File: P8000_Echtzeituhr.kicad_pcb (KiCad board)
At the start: 2 copper layers, 106.7 x 40.6 mm, 36 parts, among them X1 Socket-DIN41612-96Pin-3row

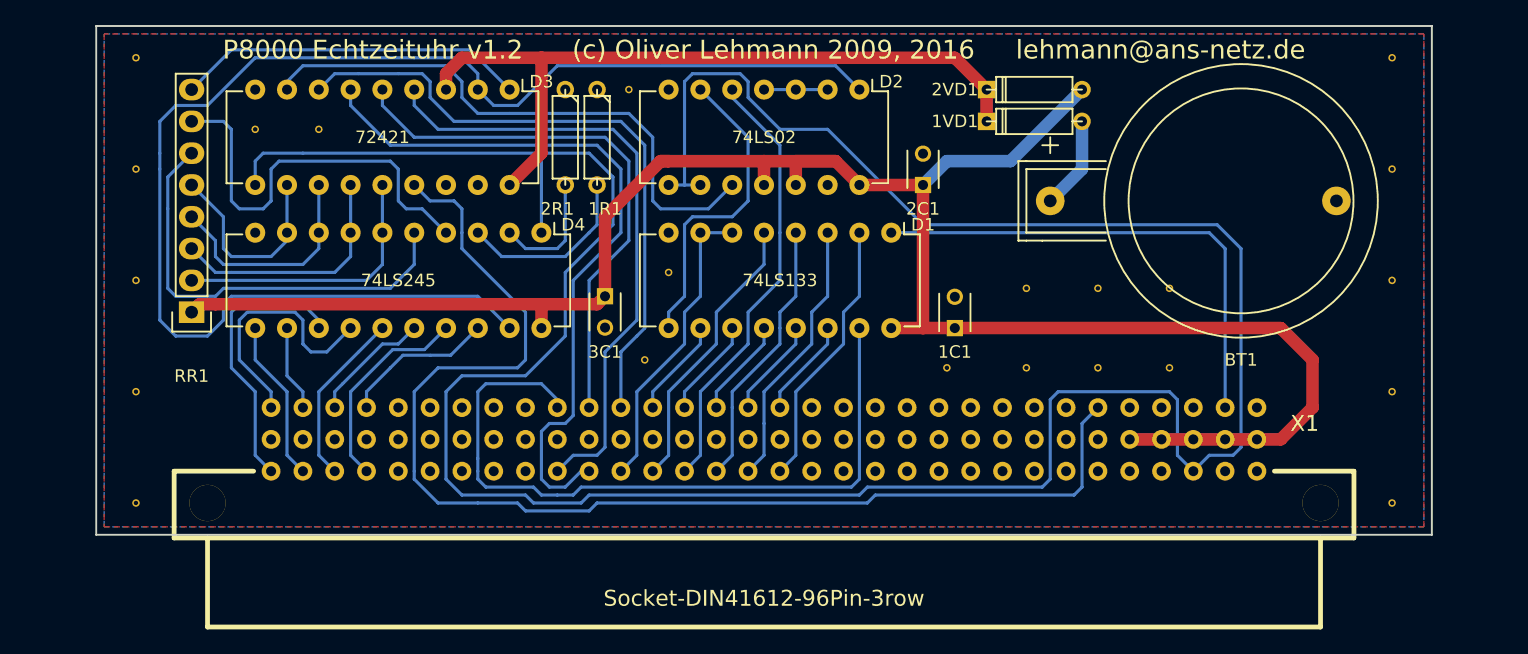
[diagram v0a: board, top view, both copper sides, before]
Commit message: fix errors from version 1.1
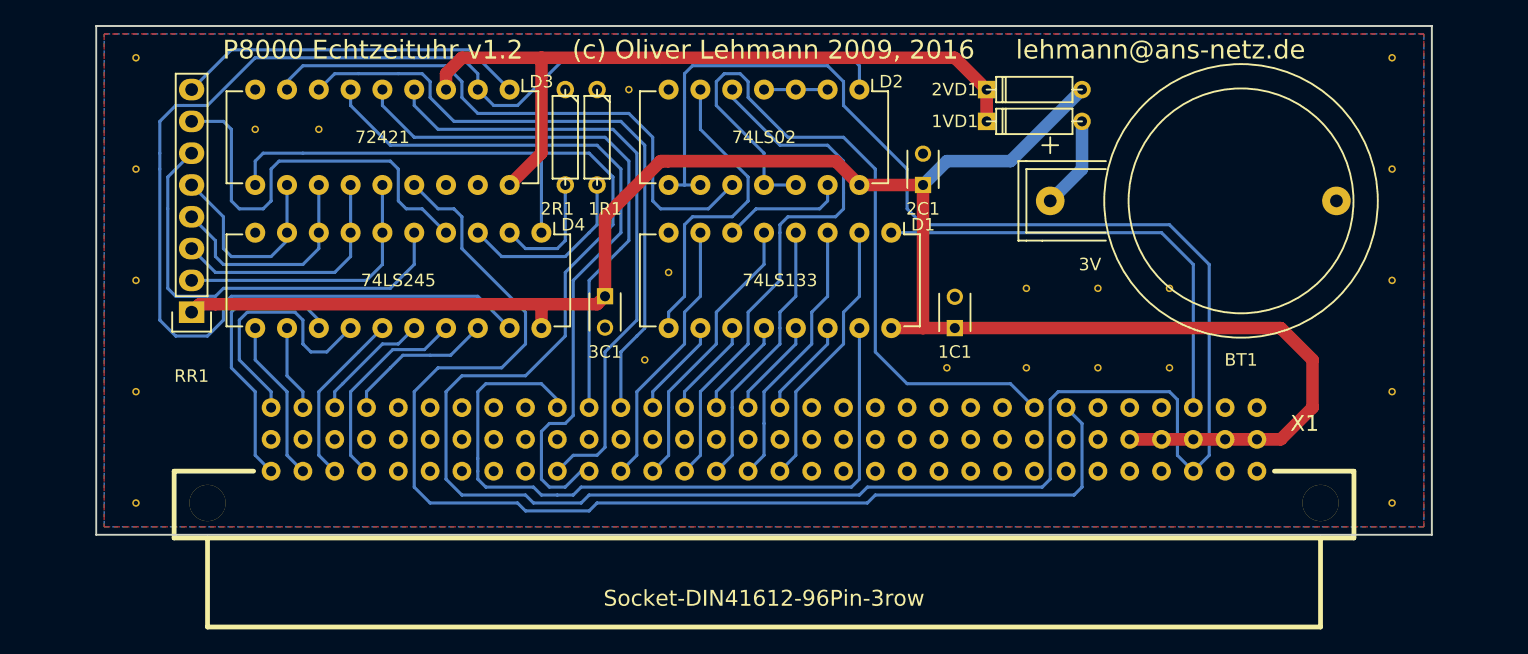
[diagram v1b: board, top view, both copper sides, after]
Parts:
- RR1: value RR7 -> 4k7
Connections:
- D1 pad 6: /A5 -> Net-(D1-Pad6)
- D2 pad 11: VCC -> //I/O
- D2 pad 12: VCC -> //I/O
- D2 pad 13: Net-(D2-Pad13) -> Net-(D1-Pad6)
- X1 pad 2c: //B/W -> Net-(X1-Pad2c)
- X1 pad 3c: Net-(X1-Pad3c) -> //B/W
- X1 pad 6c: //MRESET -> Net-(X1-Pad6c)
- X1 pad 7c: Net-(X1-Pad7c) -> //MRESET
- X1 pad 8c: Net-(X1-Pad8c) -> //I/O
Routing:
- net //I/O: track 0.00 -> 58.4 mm
- net Net-(D1-Pad6): track 0.00 -> 9.94 mm
- net /A9: track 35.2 -> 43.9 mm
- net VCC: track 158.9 -> 151.9 mm
- net //B/W: track 39.9 -> 36.6 mm
- net /A5: track 24.2 -> 21.7 mm
- net //R/W: track 226.1 -> 223.8 mm
- net Net-(D2-Pad1): track 109.9 -> 111.5 mm
- net //MRESET: track 97.8 -> 97.0 mm
